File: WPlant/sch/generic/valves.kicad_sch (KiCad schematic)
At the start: 22 parts, among them J6 Conn_01x08_Pin, Q1 FDS9926A, Q2 FDS9926A, Q3 FDS9926A, Q4 FDS9926A, U7 74HC594

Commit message: Almost finished WP Generic
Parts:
- C34: footprint (none) -> Capacitor_SMD:C_0603_1608Metric_Pad1.08x0.95mm_HandSolder
- D3, D4, D5, D6, D7, D8: value D -> ES3A; footprint (none) -> Diode_SMD:D_SMC
- D9: footprint (none) -> Diode_SMD:D_SMC
- R23, R24, R25, R26, R27, R28, R29, R30: footprint (none) -> Resistor_SMD:R_0603_1608Metric_Pad0.98x0.95mm_HandSolder
- U7: footprint (none) -> easyeda2kicad:SOIC-16_L9.9-W3.9-P1.27-LS6.0-BL
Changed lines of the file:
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@@
 			)
 		)
-		(property "Footprint" ""
+		(property "Footprint" "Resistor_SMD:R_0603_1608Metric_Pad0.98x0.95mm_HandSolder"
 			(at 119.38 28.448 90)
 			(effects
@@
 			)
 		)
-		(property "Footprint" ""
+		(property "Footprint" "Resistor_SMD:R_0603_1608Metric_Pad0.98x0.95mm_HandSolder"
 			(at 45.72 161.798 90)
 			(effects
@@
 			)
 		)
-		(property "Footprint" ""
+		(property "Footprint" "Resistor_SMD:R_0603_1608Metric_Pad0.98x0.95mm_HandSolder"
 			(at 45.72 133.858 90)
 			(effects
@@
 			)
 		)
-		(property "Footprint" ""
+		(property "Footprint" "Resistor_SMD:R_0603_1608Metric_Pad0.98x0.95mm_HandSolder"
 			(at 119.38 81.788 90)
 			(effects
@@
 			)
 		)
-		(property "Value" "D"
+		(property "Value" "ES3A"
 			(at 158.75 109.2199 90)
 			(effects
@@
 			)
 		)
-		(property "Footprint" ""
+		(property "Footprint" "Diode_SMD:D_SMC"
 			(at 156.21 107.95 0)
 			(effects
@@
 			)
 		)
-		(property "Footprint" ""
+		(property "Footprint" "Diode_SMD:D_SMC"
 			(at 82.55 132.08 0)
 			(effects
@@
 			)
 		)
-		(property "Footprint" ""
+		(property "Footprint" "Capacitor_SMD:C_0603_1608Metric_Pad1.08x0.95mm_HandSolder"
 			(at 36.5252 39.37 0)
 			(effects
@@
 			)
 		)
-		(property "Footprint" ""
+		(property "Footprint" "Resistor_SMD:R_0603_1608Metric_Pad0.98x0.95mm_HandSolder"
 			(at 119.38 136.398 90)
 			(effects
@@
 			)
 		)
-		(property "Footprint" ""
+		(property "Footprint" "easyeda2kicad:SOIC-16_L9.9-W3.9-P1.27-LS6.0-BL"
 			(at 69.85 85.09 0)
 			(effects
@@
 			)
 		)
-		(property "Value" "D"
+		(property "Value" "ES3A"
 			(at 158.75 27.9399 90)
 			(effects
@@
 			)
 		)
-		(property "Footprint" ""
+		(property "Footprint" "Diode_SMD:D_SMC"
 			(at 156.21 26.67 0)
 			(effects
@@
 			)
 		)
-		(property "Value" "D"
+		(property "Value" "ES3A"
 			(at 158.75 55.8799 90)
 			(effects
@@
 			)
 		)
-		(property "Footprint" ""
+		(property "Footprint" "Diode_SMD:D_SMC"
 			(at 156.21 54.61 0)
 			(effects
@@
 			)
 		)
-		(property "Value" "D"
+		(property "Value" "ES3A"
 			(at 158.75 135.8899 90)
 			(effects
@@
 			)
 		)
-		(property "Footprint" ""
+		(property "Footprint" "Diode_SMD:D_SMC"
 			(at 156.21 134.62 0)
 			(effects
@@
 			)
 		)
-		(property "Footprint" ""
+		(property "Footprint" "Resistor_SMD:R_0603_1608Metric_Pad0.98x0.95mm_HandSolder"
 			(at 119.38 109.728 90)
 			(effects
@@
 			)
 		)
-		(property "Footprint" ""
+		(property "Footprint" "Resistor_SMD:R_0603_1608Metric_Pad0.98x0.95mm_HandSolder"
 			(at 119.38 164.338 90)
 			(effects
@@
 			)
 		)
-		(property "Value" "D"
+		(property "Value" "ES3A"
 			(at 158.75 163.8299 90)
 			(effects
@@
 			)
 		)
-		(property "Footprint" ""
+		(property "Footprint" "Diode_SMD:D_SMC"
 			(at 156.21 162.56 0)
 			(effects
@@
 			)
 		)
-		(property "Footprint" ""
+		(property "Footprint" "Resistor_SMD:R_0603_1608Metric_Pad0.98x0.95mm_HandSolder"
 			(at 119.38 56.388 90)
 			(effects
@@
 			)
 		)
-		(property "Value" "D"
+		(property "Value" "ES3A"
 			(at 158.75 81.2799 90)
 			(effects
@@
 			)
 		)
-		(property "Footprint" ""
+		(property "Footprint" "Diode_SMD:D_SMC"
 			(at 156.21 80.01 0)
 			(effects

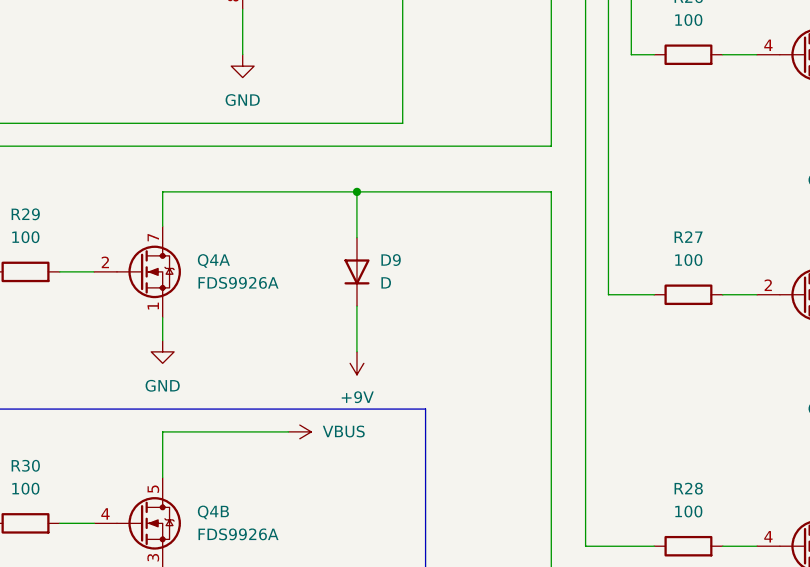
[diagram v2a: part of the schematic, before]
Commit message: Update WP Generic packages assignment
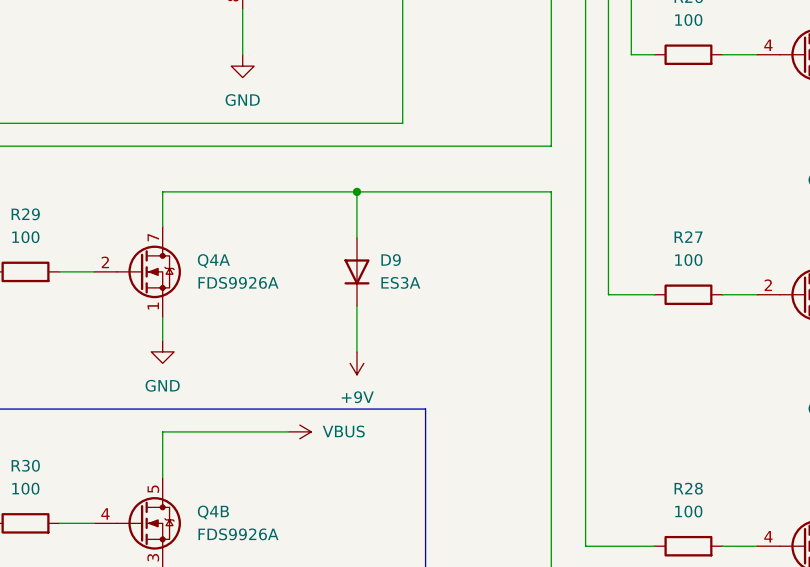
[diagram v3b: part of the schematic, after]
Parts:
- D9: value D -> ES3A
- J6: footprint (none) -> easyeda2kicad:CONN-TH_8P-P2.50_XAD-8A
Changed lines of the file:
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@@
 			)
 		)
-		(property "Footprint" ""
+		(property "Footprint" "easyeda2kicad:CONN-TH_8P-P2.50_XAD-8A"
 			(at 212.09 93.98 0)
 			(effects
@@
 			)
 		)
-		(property "Value" "D"
+		(property "Value" "ES3A"
 			(at 85.09 133.3499 90)
 			(effects
